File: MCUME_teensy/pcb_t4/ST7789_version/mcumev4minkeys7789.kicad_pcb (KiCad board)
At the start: 2 copper layers, 130.4 x 68.8 mm, 1 part

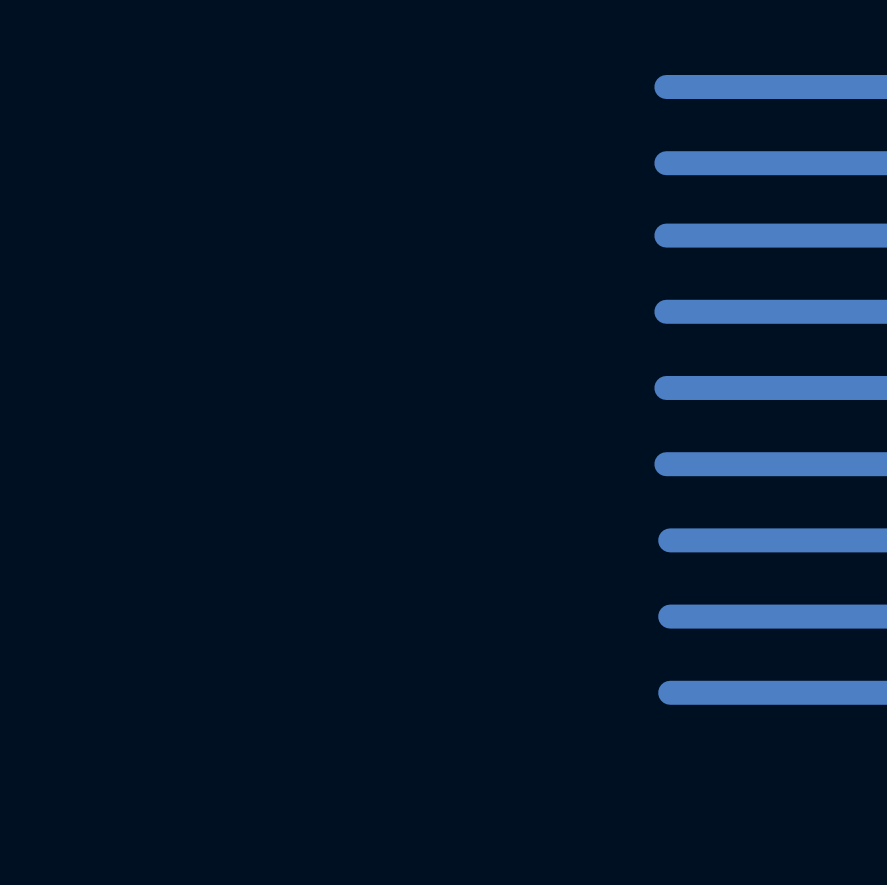
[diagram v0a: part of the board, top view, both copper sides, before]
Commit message: add msx computer
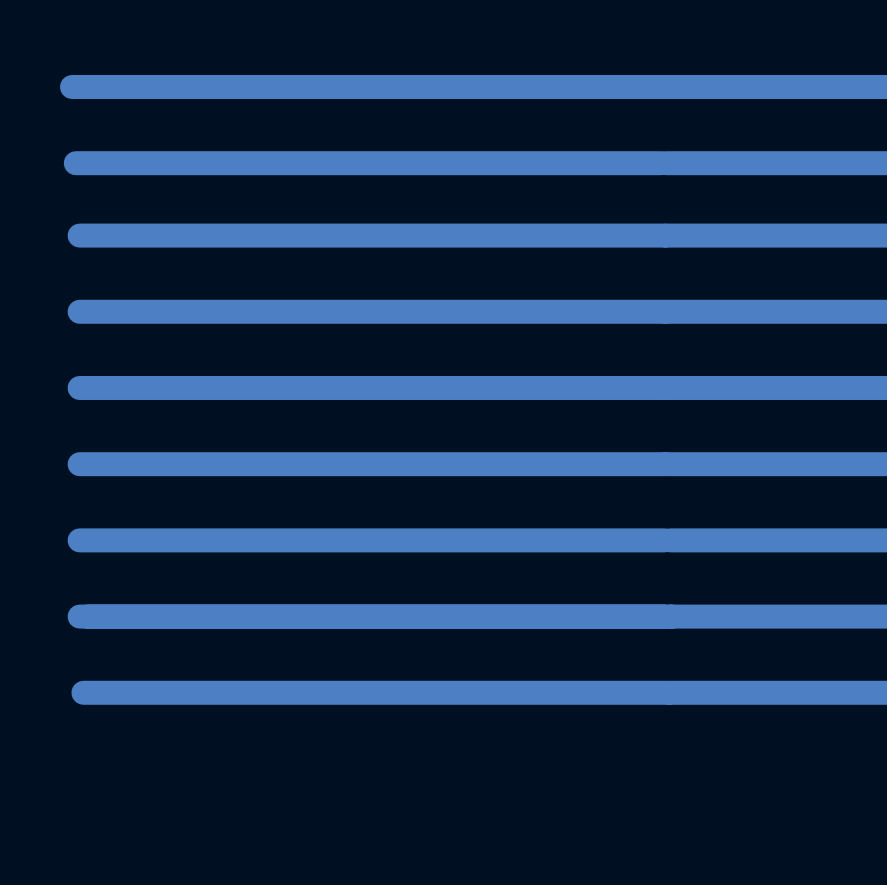
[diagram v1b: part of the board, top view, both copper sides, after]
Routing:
- net (no net): track 2174.5 -> 2388.9 mm
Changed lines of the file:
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@@
     (thickness 1.6)
     (drawings 12)
-    (tracks 1131)
+    (tracks 1142)
     (zones 0)
     (modules 1)
@@
   (segment (start 138.43 55.245) (end 144.907 48.768) (width 0.59944) (layer B.Cu) (net 0))
   (segment (start 145.415 47.625) (end 144.907 48.133) (width 0.59944) (layer B.Cu) (net 0))
+  (segment (start 58.801 21.911625) (end 39.302375 21.911625) (width 0.8) (layer B.Cu) (net 0))
+  (segment (start 58.928 24.451625) (end 39.429375 24.451625) (width 0.8) (layer B.Cu) (net 0))
+  (segment (start 59.055 26.864625) (end 39.556375 26.864625) (width 0.8) (layer B.Cu) (net 0))
+  (segment (start 59.055 29.404625) (end 39.556375 29.404625) (width 0.8) (layer B.Cu) (net 0))
+  (segment (start 59.055 31.944625) (end 39.556375 31.944625) (width 0.8) (layer B.Cu) (net 0))
+  (segment (start 59.055 34.484625) (end 39.556375 34.484625) (width 0.8) (layer B.Cu) (net 0))
+  (segment (start 59.055 37.024625) (end 39.556375 37.024625) (width 0.8) (layer B.Cu) (net 0))
+  (segment (start 59.055 39.564625) (end 39.556375 39.564625) (width 0.8) (layer B.Cu) (net 0))
+  (segment (start 59.182 42.104625) (end 39.683375 42.104625) (width 0.8) (layer B.Cu) (net 0))
+  (segment (start 59.309 39.564625) (end 39.810375 39.564625) (width 0.8) (layer B.Cu) (net 0))
+  (segment (start 60.071 21.911625) (end 40.572375 21.911625) (width 0.8) (layer B.Cu) (net 0))
 )
